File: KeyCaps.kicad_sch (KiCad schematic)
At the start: 48 parts

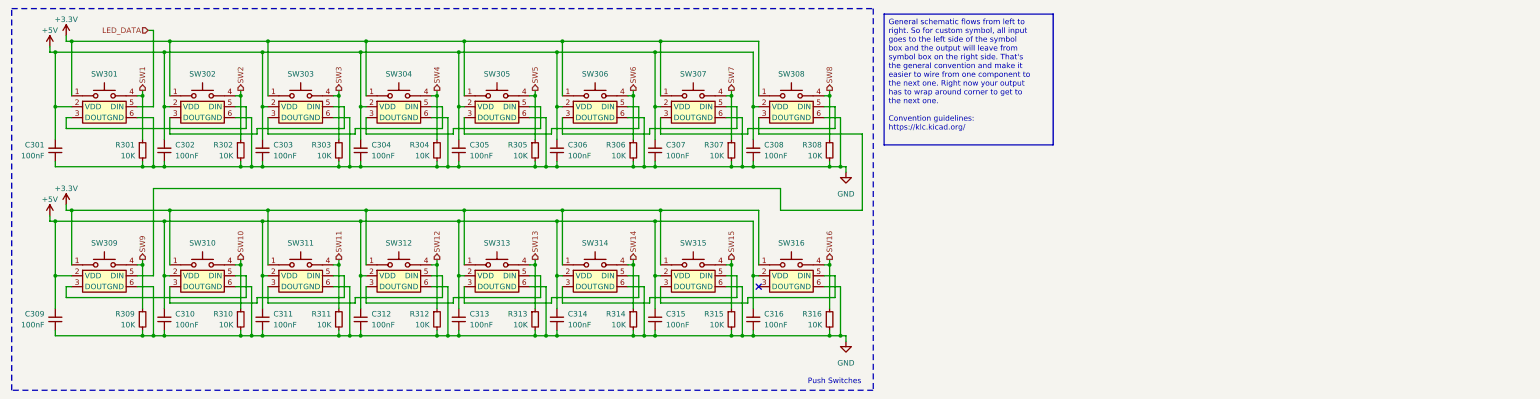
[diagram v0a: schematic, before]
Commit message: Made changes based on Josh's comments & switched to Switched to WS2812B-2020
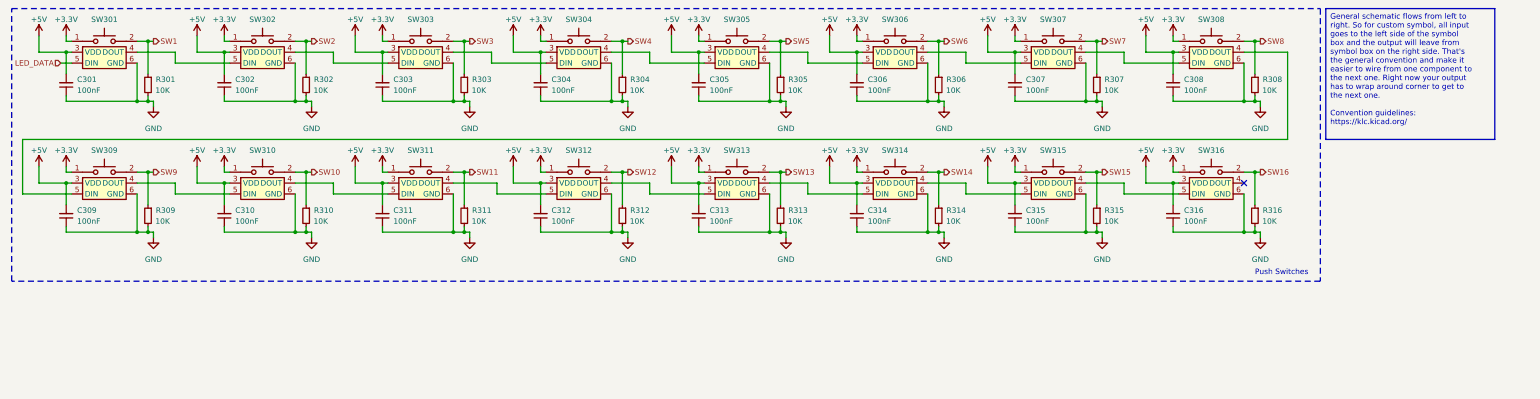
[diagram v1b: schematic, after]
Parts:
- removed SW301, SW302, SW303, SW304, SW305, SW306, SW307, SW308, SW309, SW310, SW311, SW312, SW313, SW314, SW315, SW316: ~, Adam_Custom_Footprints:CherryMX_1.00u_PCB_SK6812-EC20, symbol CherryMX_SK6812-EC20:CherryMX_SK6812-EC20
- added SW301, SW302, SW303, SW304, SW305, SW306, SW307, SW308, SW309, SW310, SW311, SW312, SW313, SW314, SW315, SW316: ~, Adam_Custom_Footprints:CherryMX_1.00u_PCB_WS2812B-2020, symbol CherryMX_WS2812B-2020:CherryMX_WS2812B-2020
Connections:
- net +3.3V: now also SW301.1, SW302.1, SW303.1, SW304.1, SW305.1, SW306.1, SW307.1, SW308.1, SW309.1, SW310.1, SW311.1, SW312.1, SW313.1, SW314.1, SW315.1, SW316.1
- net +5V: now also SW301.3 (VDD), SW302.3 (VDD), SW303.3 (VDD), SW304.3 (VDD), SW305.3 (VDD), SW306.3 (VDD), SW307.3 (VDD), SW308.3 (VDD), SW309.3 (VDD), SW310.3 (VDD), SW311.3 (VDD), SW312.3 (VDD), SW313.3 (VDD), SW314.3 (VDD), SW315.3 (VDD), SW316.3 (VDD)
- net GND: now also SW301.6 (GND), SW302.6 (GND), SW303.6 (GND), SW304.6 (GND), SW305.6 (GND), SW306.6 (GND), SW307.6 (GND), SW308.6 (GND), SW309.6 (GND), SW310.6 (GND), SW311.6 (GND), SW312.6 (GND), SW313.6 (GND), SW314.6 (GND), SW315.6 (GND), SW316.6 (GND)
- net LED_DATA: now also SW301.5 (DIN)
- net SW1: now also SW301.2
- net SW10: now also SW310.2
- net SW11: now also SW311.2
- net SW12: now also SW312.2
- net SW13: now also SW313.2
- net SW14: now also SW314.2
- net SW15: now also SW315.2
- net SW16: now also SW316.2
- net SW2: now also SW302.2
- net SW3: now also SW303.2
- net SW4: now also SW304.2
- net SW5: now also SW305.2
- net SW6: now also SW306.2
- net SW7: now also SW307.2
- net SW8: now also SW308.2
- net SW9: now also SW309.2
- new net: SW313.4 (DOUT), SW314.5 (DIN)
- new net: SW312.4 (DOUT), SW313.5 (DIN)
- new net: SW311.4 (DOUT), SW312.5 (DIN)
- new net: SW304.4 (DOUT), SW305.5 (DIN)
- new net: SW303.4 (DOUT), SW304.5 (DIN)
- new net: SW302.4 (DOUT), SW303.5 (DIN)
- new net: SW301.4 (DOUT), SW302.5 (DIN)
- new net: SW309.4 (DOUT), SW310.5 (DIN)
- new net: SW308.4 (DOUT), SW309.5 (DIN)
- new net: SW305.4 (DOUT), SW306.5 (DIN)
- new net: SW314.4 (DOUT), SW315.5 (DIN)
- new net: SW315.4 (DOUT), SW316.5 (DIN)
- new net: SW307.4 (DOUT), SW308.5 (DIN)
- new net: SW310.4 (DOUT), SW311.5 (DIN)
- new net: SW306.4 (DOUT), SW307.5 (DIN)

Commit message: Fixed LED Schematic & added 2 more LEDs
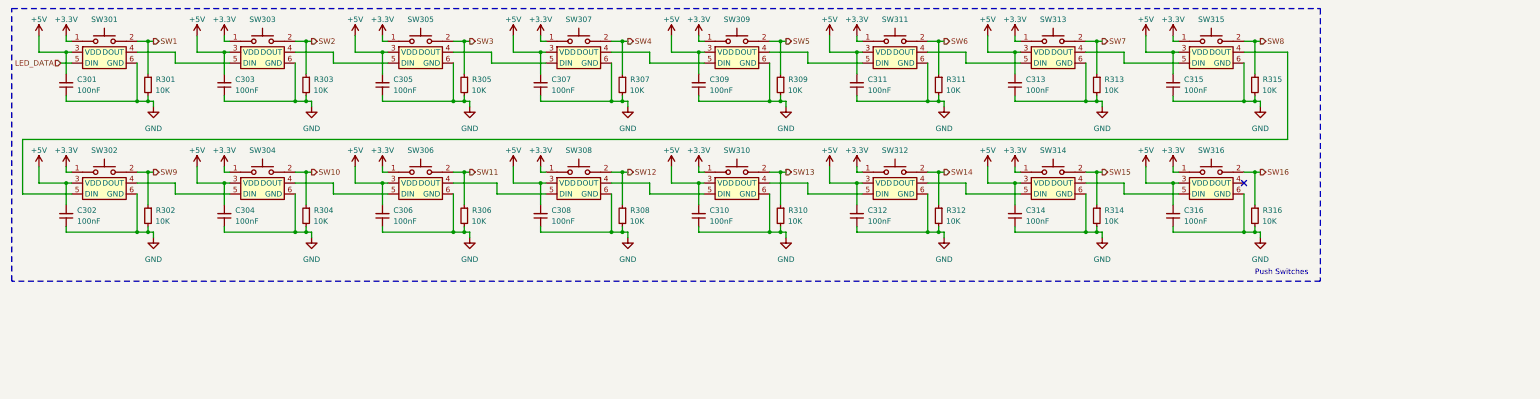
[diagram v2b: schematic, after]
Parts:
- renumbered C309 to C302, C302 to C303, C310 to C304, C303 to C305, C311 to C306, C304 to C307, C312 to C308, C305 to C309, C313 to C310, C306 to C311, C314 to C312, C307 to C313, C315 to C314, C308 to C315, R309 to R302, R302 to R303, R310 to R304, R303 to R305, R311 to R306, R304 to R307, R312 to R308, R305 to R309, R313 to R310, R306 to R311, R314 to R312, R307 to R313, R315 to R314, R308 to R315, SW309 to SW302, SW302 to SW303, SW310 to SW304, SW303 to SW305, SW311 to SW306, SW304 to SW307, SW312 to SW308, SW305 to SW309, SW313 to SW310, SW306 to SW311, SW314 to SW312, SW307 to SW313, SW315 to SW314, SW308 to SW315

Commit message: Updated PCB layout (no wires yet)
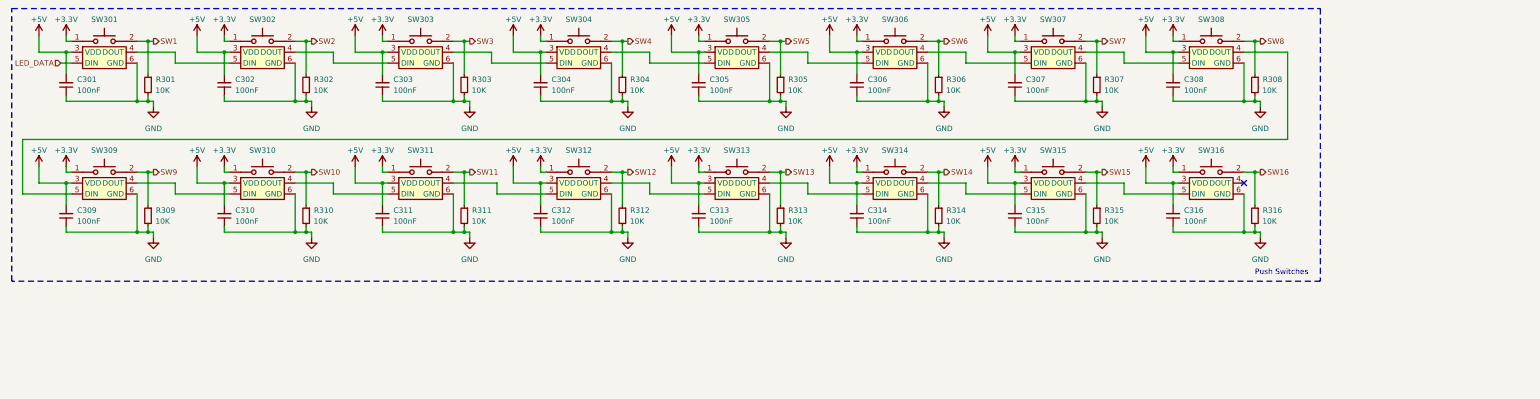
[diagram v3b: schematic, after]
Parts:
- renumbered C303 to C302, C305 to C303, C307 to C304, C309 to C305, C311 to C306, C313 to C307, C315 to C308, C302 to C309, C304 to C310, C306 to C311, C308 to C312, C310 to C313, C312 to C314, C314 to C315, R303 to R302, R305 to R303, R307 to R304, R309 to R305, R311 to R306, R313 to R307, R315 to R308, R302 to R309, R304 to R310, R306 to R311, R308 to R312, R310 to R313, R312 to R314, R314 to R315, SW303 to SW302, SW305 to SW303, SW307 to SW304, SW309 to SW305, SW311 to SW306, SW313 to SW307, SW315 to SW308, SW302 to SW309, SW304 to SW310, SW306 to SW311, SW308 to SW312, SW310 to SW313, SW312 to SW314, SW314 to SW315
